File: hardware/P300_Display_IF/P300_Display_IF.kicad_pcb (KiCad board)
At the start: 2 copper layers, 3 parts, among them J15 TFT Display 1, J16 TFT Display 2

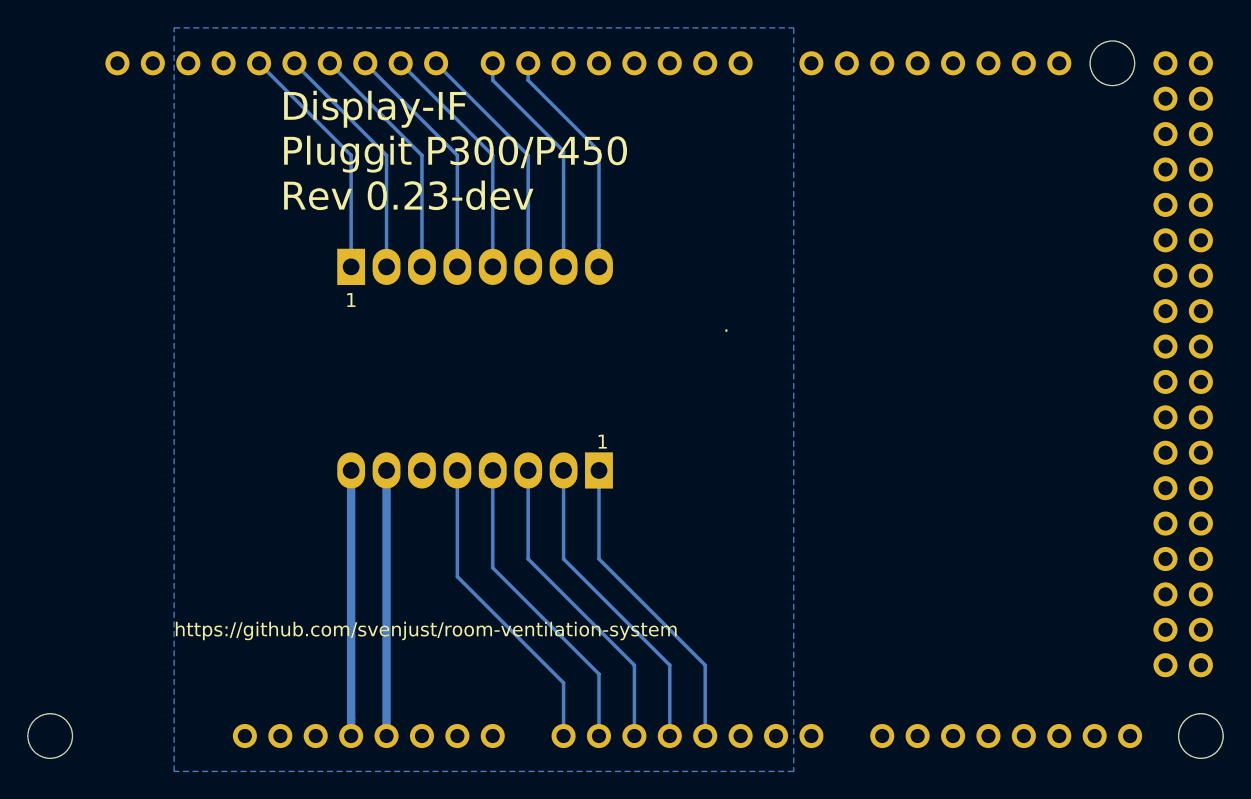
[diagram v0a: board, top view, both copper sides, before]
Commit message: P300_Display_IF: Bohrlöcher für Befestigung hinzugefügt
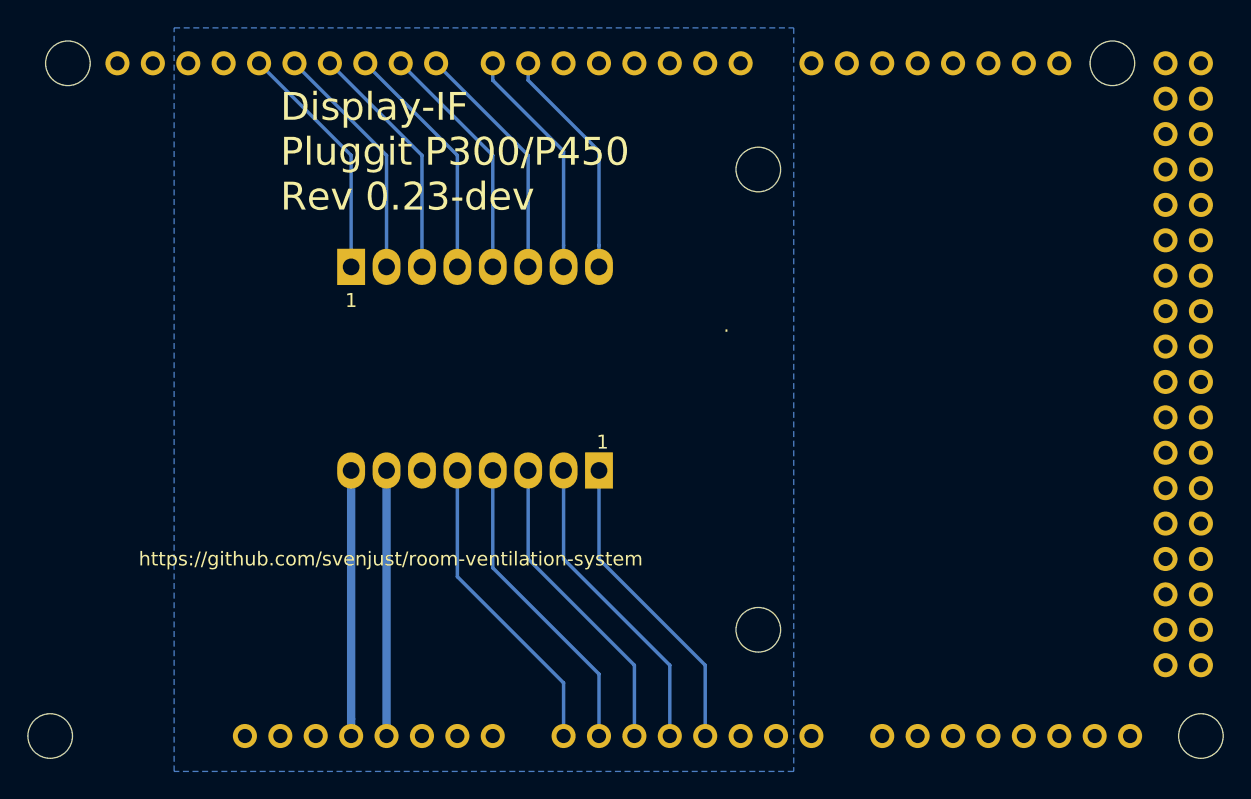
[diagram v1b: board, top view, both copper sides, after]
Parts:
- added ?: MountingHole_3.2mm_M3_DIN965, Mounting_Holes:MountingHole_3.2mm_M3_DIN965, F.Cu at (91.4, 71.1)
- added ?: MountingHole_3.2mm_M3_DIN965, Mounting_Holes:MountingHole_3.2mm_M3_DIN965, F.Cu at (141.0, 78.7)
- added ?: MountingHole_3.2mm_M3_DIN965, Mounting_Holes:MountingHole_3.2mm_M3_DIN965, F.Cu at (141.0, 111.8)
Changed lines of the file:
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@@
     (tracks 38)
     (zones 0)
-    (modules 3)
+    (modules 6)
     (nets 86)
   )
@@
     )
   )
+  (module Mounting_Holes:MountingHole_3.2mm_M3_DIN965 (layer F.Cu)
+    (at 91.44 71.12)
+    (descr "Mounting Hole 3.2mm, no annular, M3, DIN965")
+    (tags "mounting hole 3.2mm no annular m3 din965")
+    (attr virtual)
+    (fp_text reference "" (at 0 -3.8) (layer F.SilkS)
+      (effects (font (size 1 1) (thickness 0.15)))
+    )
+    (fp_text value MountingHole_3.2mm_M3_DIN965 (at 0 3.8) (layer F.Fab)
+      (effects (font (size 1 1) (thickness 0.15)))
+    )
+    (fp_text user %R (at 0.3 0) (layer F.Fab)
+      (effects (font (size 1 1) (thickness 0.15)))
+    )
+    (fp_circle (center 0 0) (end 2.8 0) (layer Cmts.User) (width 0.15))
+    (fp_circle (center 0 0) (end 3.05 0) (layer F.CrtYd) (width 0.05))
+    (pad 1 np_thru_hole circle (at 0 0) (size 3.2 3.2) (drill 3.2) (layers *.Cu *.Mask))
+  )
+  (module Mounting_Holes:MountingHole_3.2mm_M3_DIN965 (layer F.Cu)
+    (at 140.97 78.74)
+    (descr "Mounting Hole 3.2mm, no annular, M3, DIN965")
+    (tags "mounting hole 3.2mm no annular m3 din965")
+    (attr virtual)
+    (fp_text reference "" (at 0 -3.8) (layer F.SilkS)
+      (effects (font (size 1 1) (thickness 0.15)))
+    )
+    (fp_text value MountingHole_3.2mm_M3_DIN965 (at 0 3.8) (layer F.Fab)
+      (effects (font (size 1 1) (thickness 0.15)))
+    )
+    (fp_text user %R (at 0.3 0) (layer F.Fab)
+      (effects (font (size 1 1) (thickness 0.15)))
+    )
+    (fp_circle (center 0 0) (end 2.8 0) (layer Cmts.User) (width 0.15))
+    (fp_circle (center 0 0) (end 3.05 0) (layer F.CrtYd) (width 0.05))
+    (pad 1 np_thru_hole circle (at 0 0) (size 3.2 3.2) (drill 3.2) (layers *.Cu *.Mask))
+  )
+  (module Mounting_Holes:MountingHole_3.2mm_M3_DIN965 (layer F.Cu)
+    (at 140.97 111.76)
+    (descr "Mounting Hole 3.2mm, no annular, M3, DIN965")
+    (tags "mounting hole 3.2mm no annular m3 din965")
+    (attr virtual)
+    (fp_text reference "" (at 0 -3.8) (layer F.SilkS)
+      (effects (font (size 1 1) (thickness 0.15)))
+    )
+    (fp_text value MountingHole_3.2mm_M3_DIN965 (at 0 3.8) (layer F.Fab)
+      (effects (font (size 1 1) (thickness 0.15)))
+    )
+    (fp_text user %R (at 0.3 0) (layer F.Fab)
+      (effects (font (size 1 1) (thickness 0.15)))
+    )
+    (fp_circle (center 0 0) (end 2.8 0) (layer Cmts.User) (width 0.15))
+    (fp_circle (center 0 0) (end 3.05 0) (layer F.CrtYd) (width 0.05))
+    (pad 1 np_thru_hole circle (at 0 0) (size 3.2 3.2) (drill 3.2) (layers *.Cu *.Mask))
+  )
   (gr_text 1 (at 129.794 98.298) (layer F.SilkS)
     (effects (font (size 1 1) (thickness 0.15)))
@@
     (effects (font (size 1 1) (thickness 0.2)) (justify mirror))
   )
-  (gr_text https://github.com/svenjust/room-ventilation-system (at 99.06 111.76) (layer F.SilkS)
+  (gr_text https://github.com/svenjust/room-ventilation-system (at 96.52 106.68) (layer F.SilkS)
     (effects (font (size 1 1) (thickness 0.25)) (justify left))
   )
@@
     (polygon
       (pts
-        (xy 99.06 68.58) (xy 146.05 68.58) (xy 146.05 121.92) (xy 99.06 121.92)
+        (xy 87.63 68.58) (xy 146.05 68.58) (xy 146.05 121.92) (xy 87.63 121.92)
       )
     )

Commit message: Platinen V.23 in die Herstellung gegeben
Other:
- board text added: "Display-IF Pluggit P300/P450 Rev 0.23"
- board text removed: "Display-IF Pluggit P300/P450 Rev 0.23-dev"
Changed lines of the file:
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@@
-(kicad_pcb (version 20171130) (host pcbnew "(5.0.2)-1")
+(kicad_pcb (version 20171130) (host pcbnew "(5.0.1)-3")
   (general
     (thickness 1.6)
@@
     (effects (font (size 1 1) (thickness 0.25)) (justify left))
   )
-  (gr_text "Display-IF\nPluggit P300/P450\nRev 0.23-dev" (at 106.68 77.47) (layer F.SilkS)
-    (effects (font (size 2 2) (thickness 0.3)) (justify left))
+  (gr_text "Display-IF\nPluggit P300/P450\nRev 0.23" (at 106.68 77.47) (layer F.SilkS)
+    (effects (font (size 1.4 1.4) (thickness 0.2)) (justify left))
   )
   (dimension 53.34 (width 0.3) (layer F.Fab)

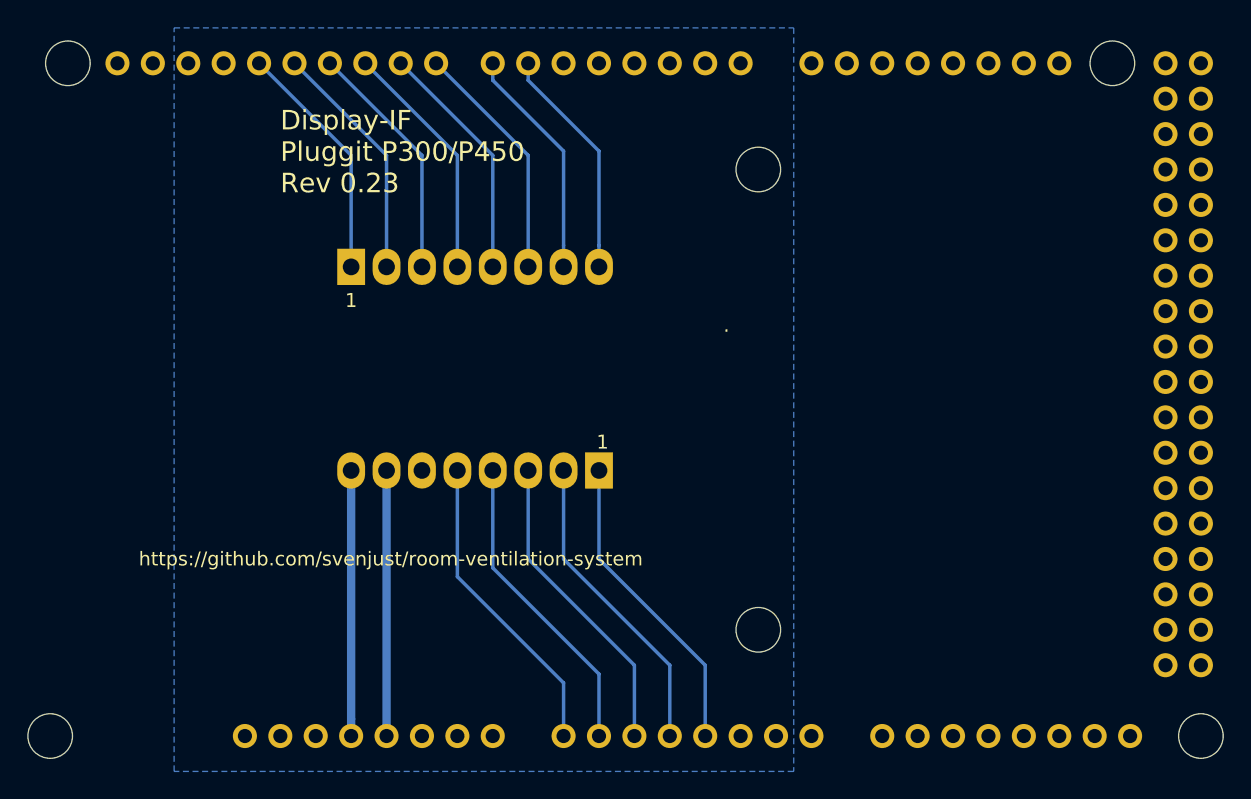
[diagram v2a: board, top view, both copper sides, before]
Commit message: Footprint Arduino reduziert
Für die Displayplatine wird nur eine Teil des Arduino Mega Footprint benötigt.
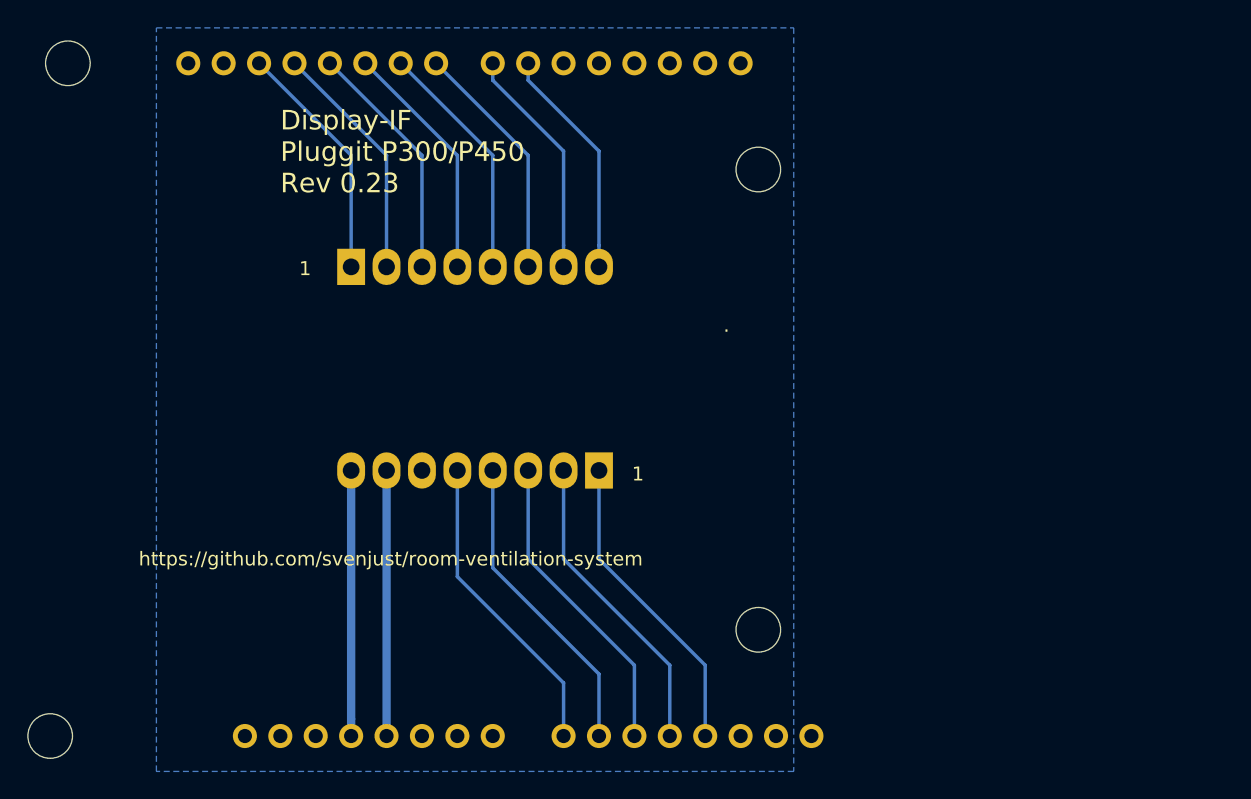
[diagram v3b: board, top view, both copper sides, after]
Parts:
- removed XA1: Arduino_Mega2560_Shield, Arduino:Arduino_Mega2560_Shield_no_ICSP
- added ?: , Arduino_Parts:Arduino_Mega2560_Shield_no_ICSP, F.Cu at (76.2, 121.9)
- ? (x3): value MountingHole_3.2mm_M3_DIN965 -> (none)
